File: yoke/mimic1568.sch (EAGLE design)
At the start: 23 parts, among them P1 1K, P2 1K, P3 44PINEDGE-M, U1 AD7533, U2 CD74HC573E, U3 CD74HCT75, U4 OPA2340N, U5 AD7533, U6 CD74HC573E

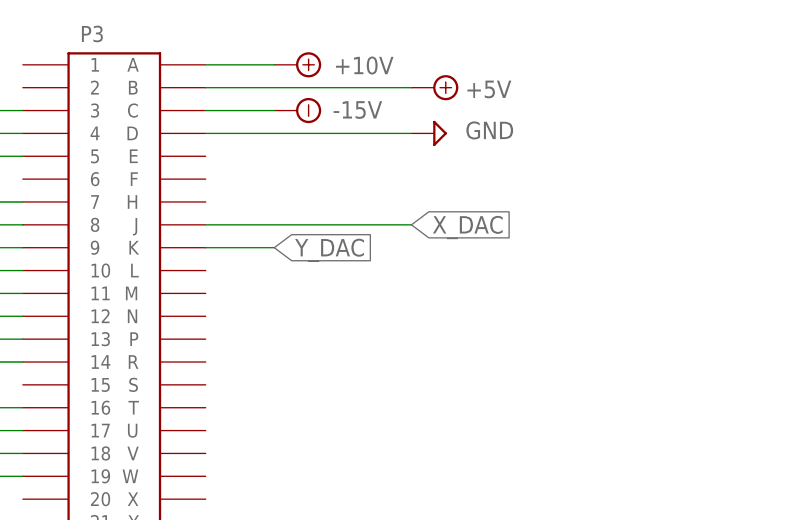
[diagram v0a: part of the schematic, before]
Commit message: added missing connector on bckplane
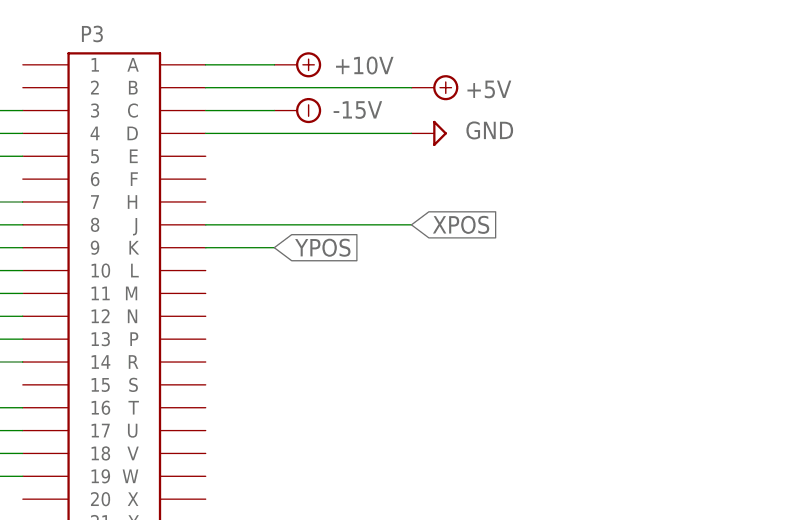
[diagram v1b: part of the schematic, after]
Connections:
- removed net X_DAC: P3.J
- removed net Y_DAC: P3.K
- net XPOS: now also P3.J
- net YPOS: now also P3.K
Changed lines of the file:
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@@
 <pinref part="R2" gate="&gt;NAME" pin="P$1"/>
+</segment>
+<segment>
+<label x="314.96" y="365.76" size="1.9304" layer="95" font="vector" ratio="10" xref="yes"/>
+<wire x1="314.96" y1="365.76" x2="292.1" y2="365.76" width="0.1524" layer="91"/>
+<pinref part="P3" gate="G$1" pin="J"/>
 </segment>
 </net>
@@
 <wire x1="398.78" y1="175.26" x2="406.4" y2="175.26" width="0.1524" layer="91"/>
 <pinref part="R3" gate="&gt;NAME" pin="P$1"/>
+</segment>
+<segment>
+<label x="299.72" y="363.22" size="1.9304" layer="95" font="vector" ratio="10" xref="yes"/>
+<wire x1="292.1" y1="363.22" x2="299.72" y2="363.22" width="0.1524" layer="91"/>
+<pinref part="P3" gate="G$1" pin="K"/>
 </segment>
 </net>
@@
 </segment>
 </net>
-<net name="X_DAC" class="0">
-<segment>
-<label x="314.96" y="365.76" size="1.9304" layer="95" font="vector" ratio="10" xref="yes"/>
-<wire x1="314.96" y1="365.76" x2="292.1" y2="365.76" width="0.1524" layer="91"/>
-<pinref part="P3" gate="G$1" pin="J"/>
-</segment>
-</net>
-<net name="Y_DAC" class="0">
-<segment>
-<label x="299.72" y="363.22" size="1.9304" layer="95" font="vector" ratio="10" xref="yes"/>
-<wire x1="292.1" y1="363.22" x2="299.72" y2="363.22" width="0.1524" layer="91"/>
-<pinref part="P3" gate="G$1" pin="K"/>
-</segment>
-</net>
